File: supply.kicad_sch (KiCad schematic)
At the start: 167 parts, among them J10001 JST_SH_1x4_BM04B-SRSS-TB-LF-SN, J1001 BarrelJack_3167288, Q10001 BSS138PW, Q10002 SI7613DN-T1-GE3, Q10003 BSS138PW, Q1001 SI7613DN-T1-GE3, Q1002 BSS138PW, Q20001 BSS138PW, SW10002 SW_CVS-08TB, SW1002 SW_KMR211NGLFS_SMD, U10001 NCP718BSN330T1G, U10002 MPM54304GMN, U10003 MPM54304GMN, U10004 MAX16150A_SOT, U10005 LTC4412IS6, U10006 LM3880, U10007 MP8869S, U10008 XC6230H001ER-G, U10009 MAX812REUS+T, U1001 LTC4412IS6, U10010 PAC1954T-E_VQFN, U10011 PAC1954T-E_VQFN, U10012 MCP4726A0T-E_MAY, U10013 TS5A3359_VSSOP, U10014 TS5A3359_VSSOP

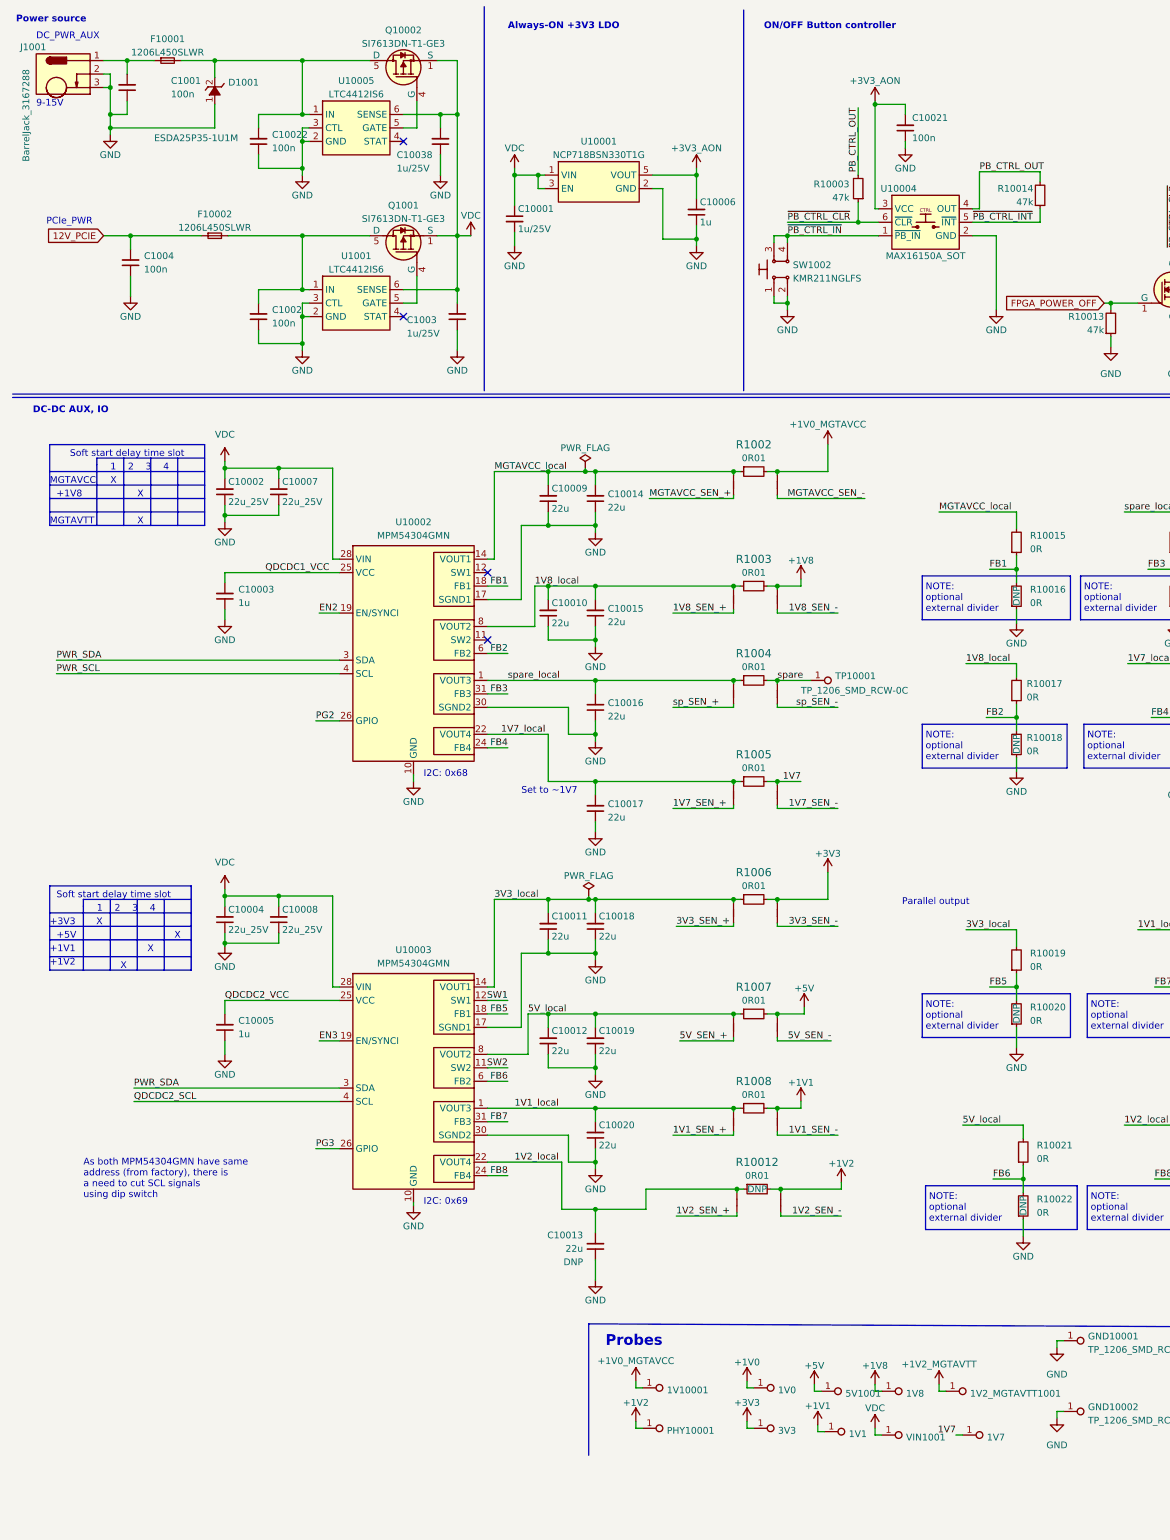
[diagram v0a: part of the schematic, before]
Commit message: Improve PCB after layout review
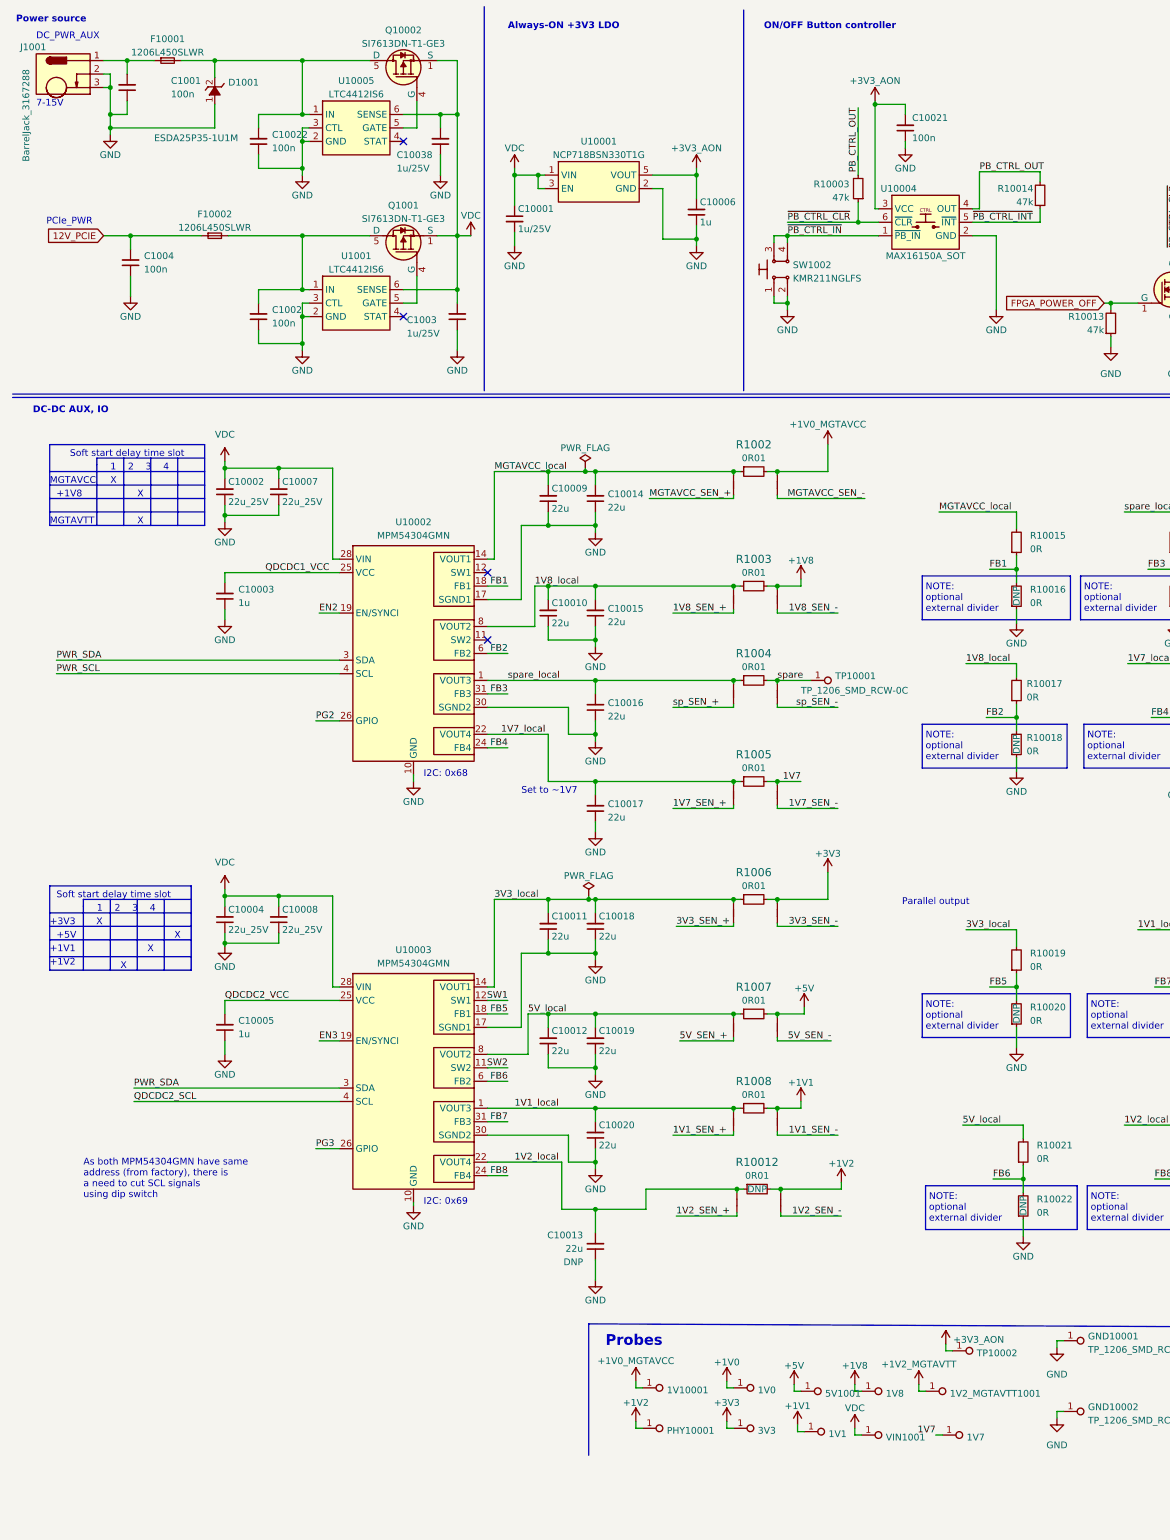
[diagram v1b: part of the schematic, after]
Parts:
- added TP10002: TP_1mm_SMD, antmicro-footprints:TP_SMD_1mm, symbol antmicroTestPoints:TP_1mm_SMD
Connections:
- net +3V3_AON: now also TP10002.1
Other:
- note added: "7-15V"
- note removed: "9-15V"
- moved on the sheet: 1V0, 1V1, 1V2_MGTAVTT1001, 1V7, 1V8, 3V3, 5V1001, VIN1001

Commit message: Re-annotate schematic
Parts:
- renumbered C1001 to C169, C1004 to C170, C10002 to C171, C10003 to C172, C10004 to C173, C10005 to C174, C10022 to C175, C1002 to C176, C10007 to C177, C10008 to C178, C10038 to C179, C1003 to C180, C10001 to C181, C10009 to C182, C10010 to C183, C10011 to C184, C10012 to C185, C10014 to C186, C10015 to C187, C10016 to C188, C10017 to C189, C10018 to C190, C10019 to C191, C10020 to C192, C10013 to C193, C10006 to C194, C10021 to C195, C10048 to C196, C10049 to C197, C10042 to C198, C10040 to C199, C10025 to C200, C10026 to C201, C10027 to C202, C10039 to C203, C10028 to C204, C10043 to C205, C10029 to C206, C10044 to C207, C10030 to C208, C10023 to C209, C10031 to C210, C10032 to C211, C10024 to C212, C10033 to C213, C10041 to C214, C10034 to C215, C10045 to C216, C10035 to C217, C10046 to C218, C10036 to C219, C10047 to C220, C10037 to C221, D1001 to D16, F10001 to F1, F10002 to F2, J1001 to J7, J10001 to J8, L1001 to L1, NT1001 to NT1, NT1009 to NT10, NT1010 to NT11, NT1011 to NT12, NT1012 to NT13, NT1013 to NT14, NT1014 to NT15, NT10002 to NT16, NT1002 to NT2, NT1003 to NT3, NT1004 to NT4, NT1005 to NT5, NT1006 to NT6, NT1007 to NT7, NT10001 to NT8, NT1008 to NT9, Q10002 to Q12, Q1001 to Q13, Q10003 to Q14, Q20001 to Q15, Q10001 to Q16, Q1002 to Q17, R10008 to R135, R10009 to R136, R10010 to R137, R10011 to R138, R10004 to R139, R10005 to R140, R1002 to R141, R1003 to R142, R1004 to R143, R1005 to R144, R1006 to R145, R1007 to R146, R1008 to R147, R10012 to R148, R10003 to R149, R10001 to R150, R10015 to R151, R10016 to R152, R10017 to R153, R10018 to R154, R10019 to R155, R10020 to R156, R10021 to R157, R10022 to R158, R10002 to R159, R10014 to R160, R10013 to R161, R10025 to R162, R10026 to R163, R10031 to R164, R10032 to R165, R10027 to R166, R10028 to R167, R10029 to R168, R10030 to R169, R20001 to R170, R10043 to R171, R10023 to R172, R10045 to R173, R10006 to R174, R10007 to R175, R10024 to R176, R10044 to R177, R10047 to R178, R10048 to R179, R10036 to R180, R10037 to R181, R10046 to R182, R10038 to R183, R10033 to R184, R10039 to R185, R10040 to R186, R10034 to R187, R10041 to R188, R10042 to R189, R10035 to R190, SW10002 to SW4, SW1002 to SW5, 1V0 to TP10, 3V3 to TP11, 5V1001 to TP12, 1V1 to TP13, TP10001 to TP14, 1V8 to TP15, VIN1001 to TP16, 1V2_MGTAVTT1001 to TP17, 1V7 to TP18, TP10002 to TP19, GND10001 to TP20, GND10002 to TP21, 1V10001 to TP8, PHY10001 to TP9, U10005 to U17, U1001 to U18, U10002 to U19, U10003 to U20, U10001 to U21, U10004 to U22, U10013 to U23, U10014 to U24, U10010 to U25, U10009 to U26, U10007 to U27, U10008 to U28, U10012 to U29, U10011 to U30, U10006 to U31
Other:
- moved on the sheet: TP19

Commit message: Add local libraries
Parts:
- C207, C211, C218: footprint antmicro-footprints:C_0402_1005Metric -> sodimm-ddr5-tester-footprints:C_0402_1005Metric; symbol antmicroCapacitors0402:C_10u_6.3V_0402 -> sodimm-ddr5-tester:C_10u_6.3V_0402
- F1, F2: footprint antmicro-footprints:F_1206_3216Metric -> sodimm-ddr5-tester-footprints:F_1206_3216Metric; symbol antmicroFuses:PTC_4.5A_1206 -> sodimm-ddr5-tester:PTC_4.5A_1206
- R136, R137, R138: footprint antmicro-footprints:R_0402_1005Metric -> sodimm-ddr5-tester-footprints:R_0402_1005Metric; symbol antmicroResistors0402:R_0R_0402 -> sodimm-ddr5-tester:R_0R_0402
- SW4: footprint antmicro-footprints:SW_DIP_SPSTx08_Slide_Copal_CVS-08xB_W5.9mm_P1mm -> sodimm-ddr5-tester-footprints:SW_DIP_SPSTx08_Slide_Copal_CVS-08xB_W5.9mm_P1mm; symbol SlideSwitches:SW_CVS-08TB -> sodimm-ddr5-tester:SW_CVS-08TB
- TP10, TP11, TP12, TP13, TP15, TP16, TP17, TP18, TP19, TP8, TP9: footprint antmicro-footprints:TP_SMD_1mm -> sodimm-ddr5-tester-footprints:TP_SMD_1mm; symbol antmicroTestPoints:TP_1mm_SMD -> sodimm-ddr5-tester:TP_1mm_SMD
- TP14, TP20, TP21: footprint antmicro-footprints:TP_1206_SMD_RCW-0C -> sodimm-ddr5-tester-footprints:TP_1206_SMD_RCW-0C; symbol antmicroTestPoints:TP_1206_SMD_RCW-0C -> sodimm-ddr5-tester:TP_1206_SMD_RCW-0C
- U23, U24: footprint antmicro-footprints:VSSOP-8_2.3x2mm_P0.5mm -> sodimm-ddr5-tester-footprints:VSSOP-8_2.3x2mm_P0.5mm; symbol antmicroInterfaceAnalogSwitchesMultiplexersDemultiplexers:TS5A3359_VSSOP -> sodimm-ddr5-tester:TS5A3359_VSSOP
- U29: footprint antmicro-footprints:DFN-6-1EP_2x2mm_P0.65mm_EP1x1.6mm -> sodimm-ddr5-tester-footprints:DFN-6-1EP_2x2mm_P0.65mm_EP1x1.6mm; symbol antmicroDataAcquisitionDigitaltoAnalogConvertersDAC:MCP4726A0T-E_MAY -> sodimm-ddr5-tester:MCP4726A0T-E_MAY
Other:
- note added: "1t2t3t4"
- note removed: "1 2 3 4"

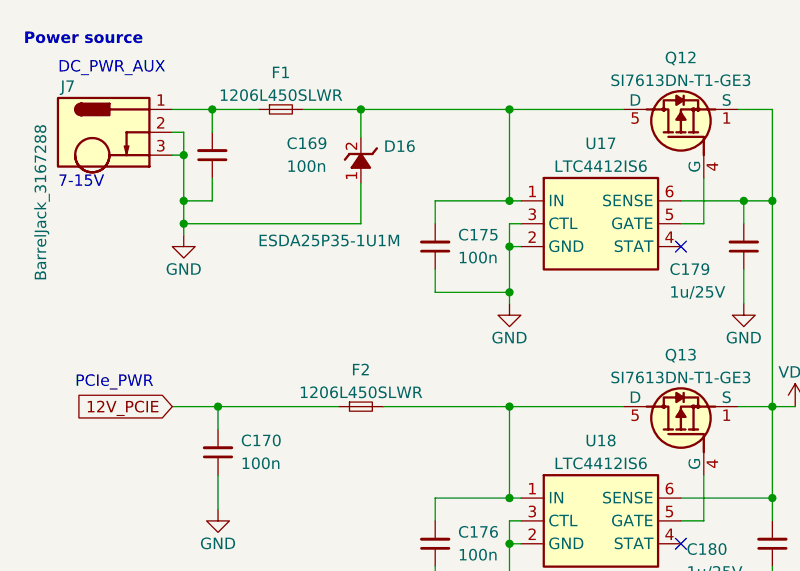
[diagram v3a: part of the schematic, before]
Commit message: Change via drill size. Replace the holes for mounting the PCIe backplate with plated ones. Move PCB SHA marking. Increase clearance to 12V planes and traces
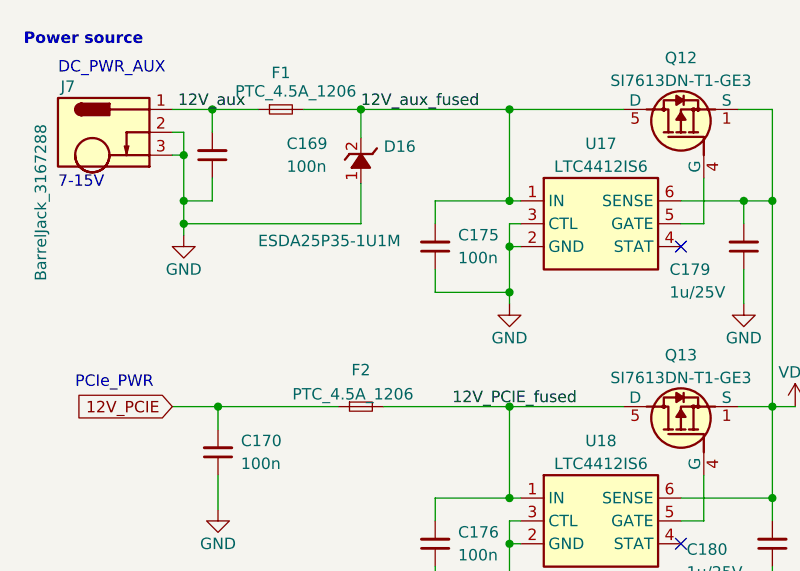
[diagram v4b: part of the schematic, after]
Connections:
- net 12V_aux: now reaches C169.2, F1.1, J7.1
- net 12V_aux_fused: now reaches C175.2, D16.2 (A), F1.2, Q12.5 (D), U17.1 (IN)
- net 12V_PCIE_fused: now reaches C176.2, F2.2, Q13.5 (D), U18.1 (IN)
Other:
- note added: "1 2 3 4"
- note removed: "1t2t3t4"

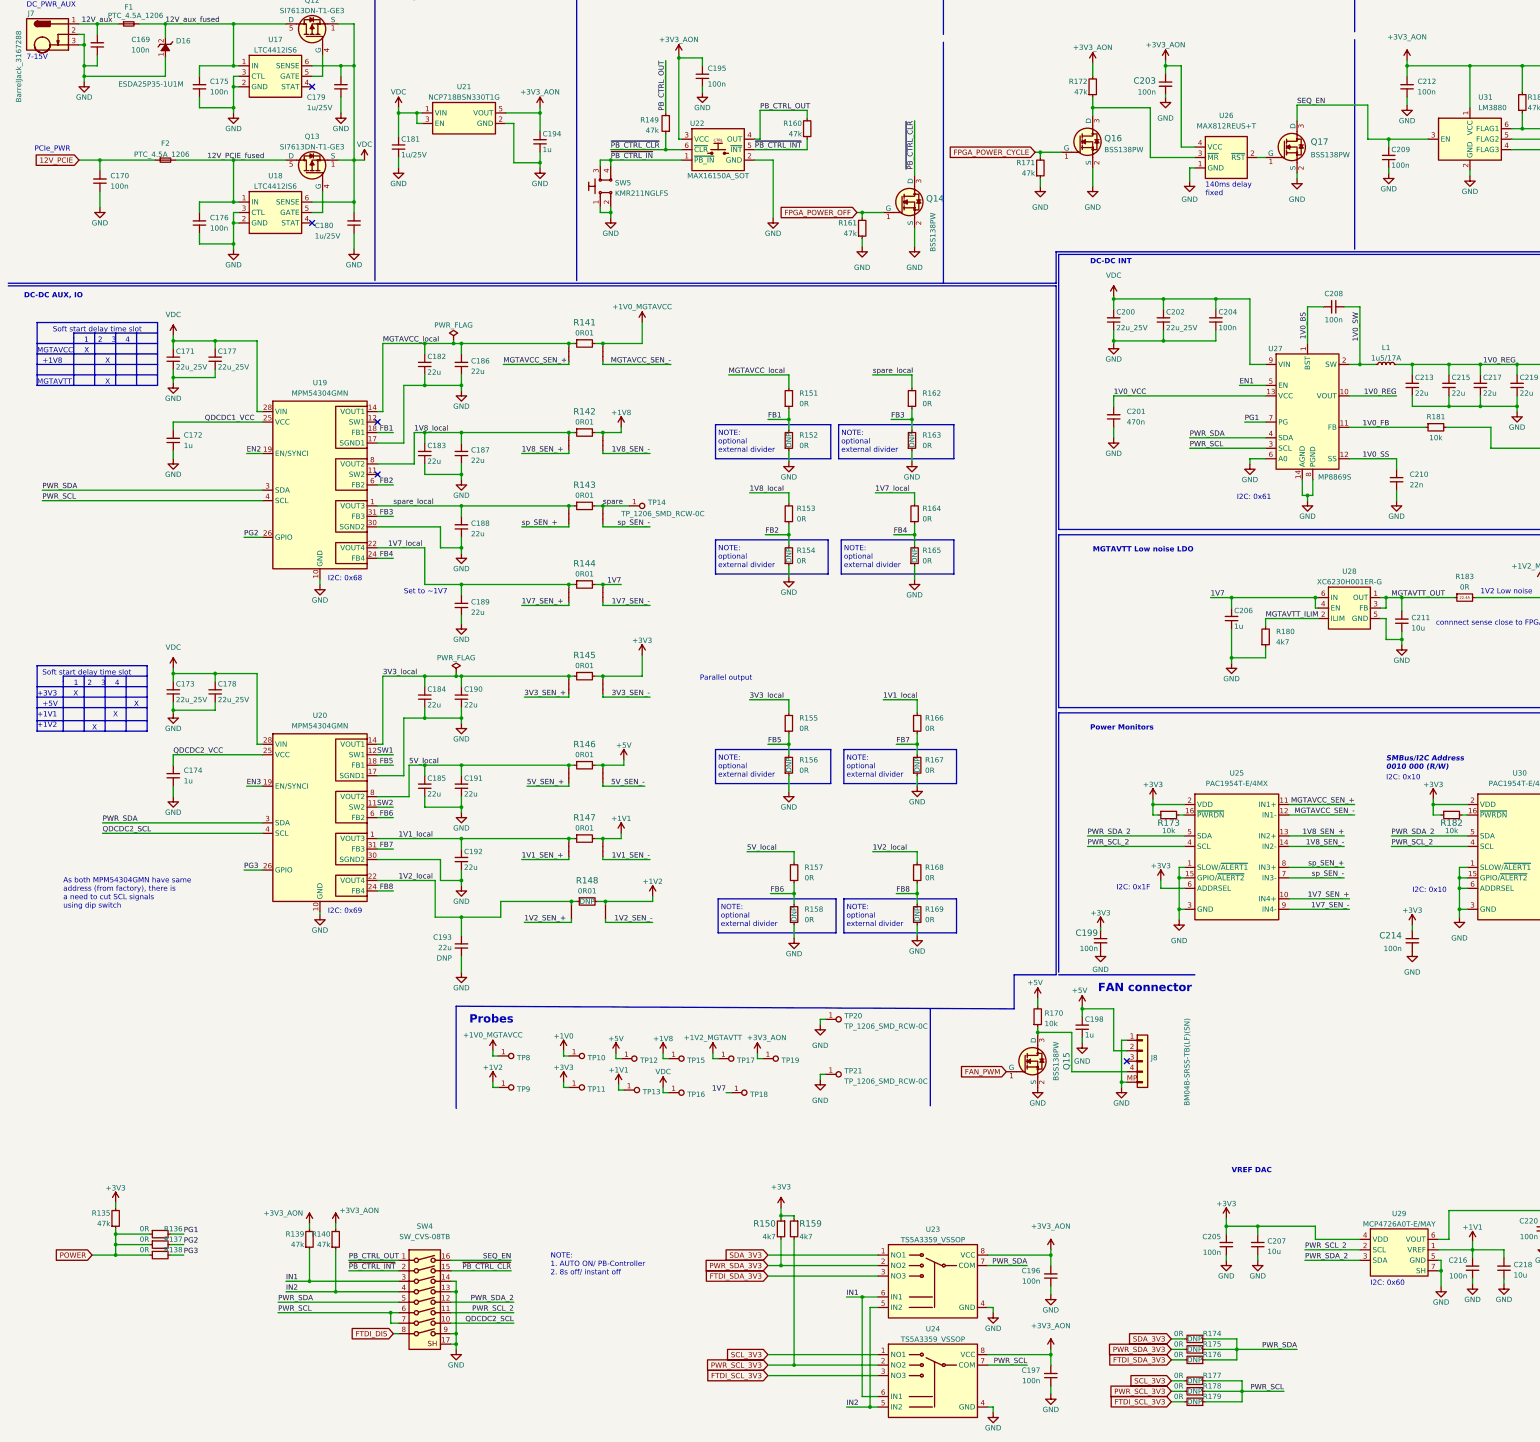
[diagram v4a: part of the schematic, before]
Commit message: Connect DDR hierarchical labels. Define and connect JTAG, RGMII, TDMS, UART, and SDIO buses. Reorganize schematic blocks between sheets
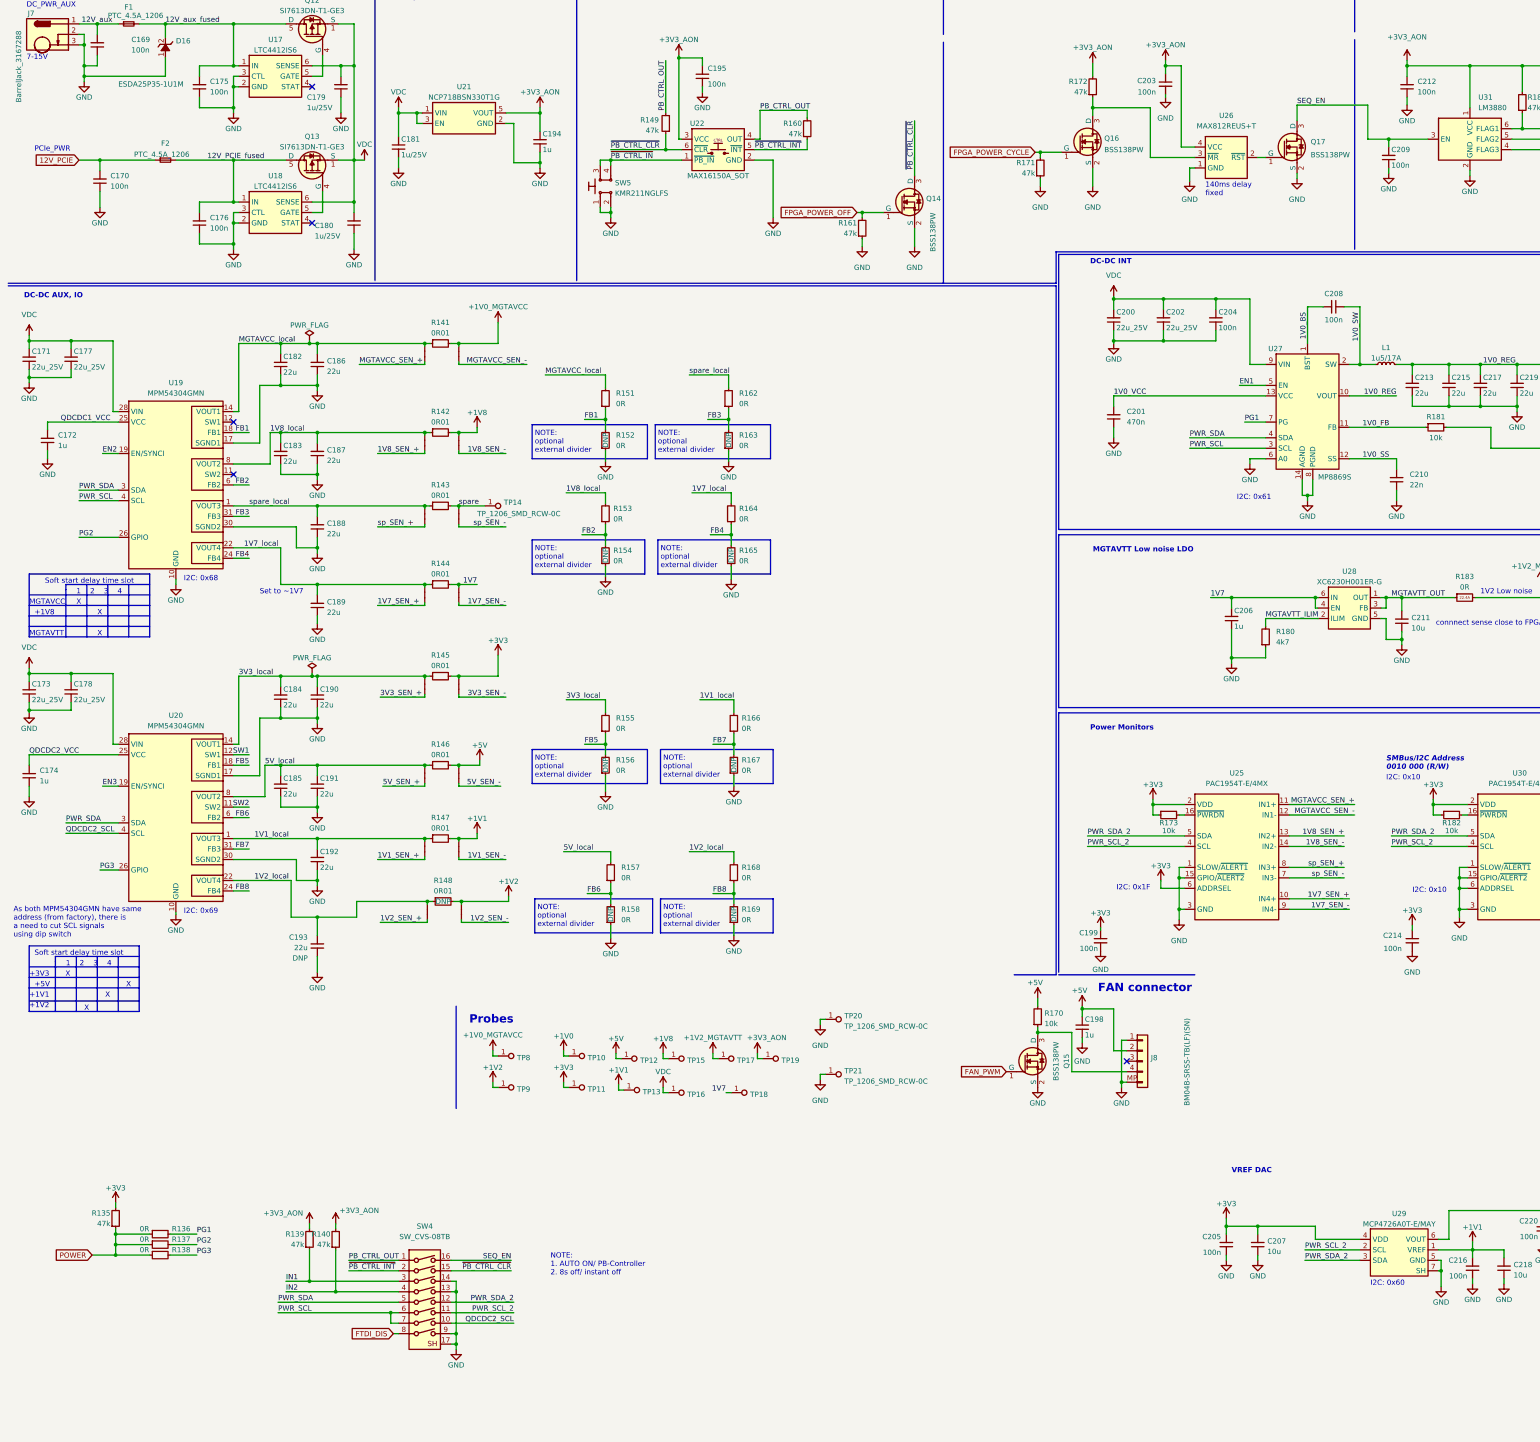
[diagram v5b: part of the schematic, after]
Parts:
- removed C196, C197: C_100n_0402, sodimm-ddr5-tester-footprints:C_0402_1005Metric, symbol sodimm-ddr5-tester:C_100n_0402
- removed R150, R159: R_4k7_0402, sodimm-ddr5-tester-footprints:R_0402_1005Metric, symbol sodimm-ddr5-tester:R_4k7_0402
- removed R174, R175, R176, R177, R178, R179: R_0R_0402, sodimm-ddr5-tester-footprints:R_0402_1005Metric, symbol sodimm-ddr5-tester:R_0R_0402
- removed U23, U24: TS5A3359_VSSOP, sodimm-ddr5-tester-footprints:VSSOP-8_2.3x2mm_P0.5mm, symbol sodimm-ddr5-tester:TS5A3359_VSSOP
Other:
- note removed: "Parallel output"
- moved on the sheet: C171, C172, C173, C174, C177, C178, C182, C183, C184, C185, C186, C187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
